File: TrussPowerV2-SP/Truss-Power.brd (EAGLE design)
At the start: 30.8 x 19 mm, 32 parts, among them J1 XF2L-0535-1, J2 XF2L-0535-1, Q1 ABM-16MHZ, SW1 LS12T2-T, SW2 EVQ11U09K, SW3 ESE31L11T, U2 TPS62200, X1 22-23-2021

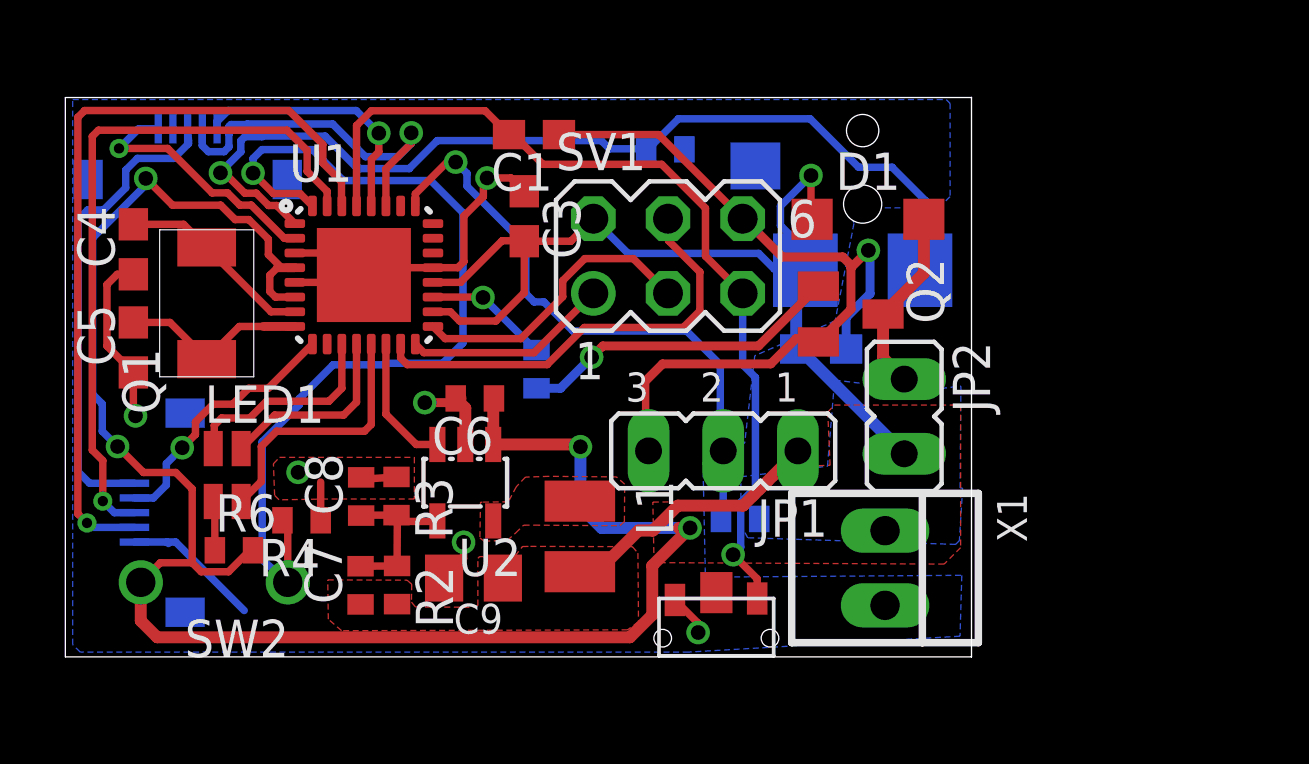
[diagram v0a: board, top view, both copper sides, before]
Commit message: Generate SP boards for Gen1
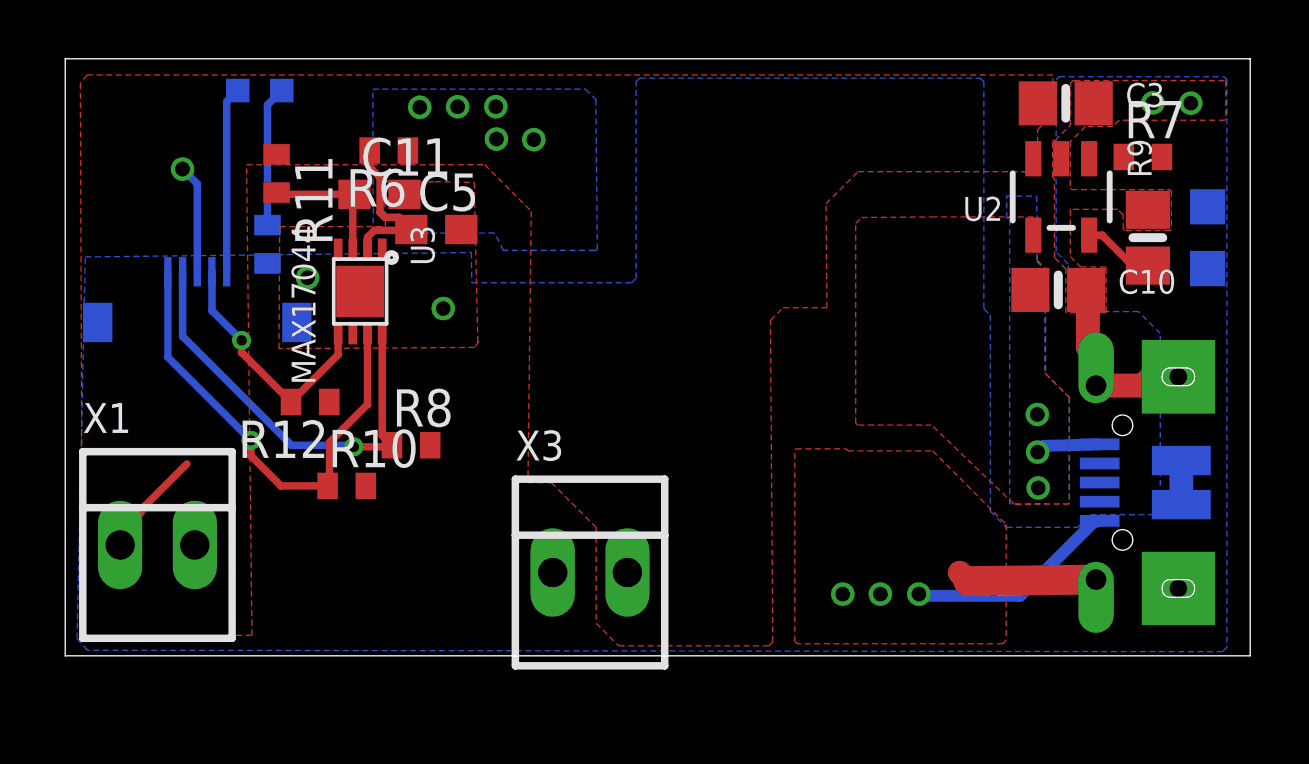
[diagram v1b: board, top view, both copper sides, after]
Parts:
- removed C1, C2: 100nF, rcl:C0603
- removed C4: 22pF, rcl:C0603
- removed C6: 4.7uF, rcl:C0402
- removed C7, C8: 100nF, rcl:C0402
- removed C9: 10uF, resistor:C0805K
- removed D1: (no value), diode:SOD123
- removed J2: XF2L-0535-1, adafruit:XF2L-0535-1
- removed JP1: MQ303B, jumper:JP2
- removed JP2: Solenoid, jumper:JP1
- removed L1: 10uH, resistor:L2825P
- removed Q1: ABM-16MHZ, NewPart:ABM-16MHZ
- removed Q2: (no value), semicon-smd-ipc:SOT23
- removed R1: 10K, resistor:R0402
- removed R2: 16K, resistor:R0402
- removed R3: 20K, resistor:R0402
- removed R4: 330, resistor:R0402
- removed R5: 2.2K, resistor:R0402
- removed SV1: (no value), con-lstb:MA03-2
- removed SW1: LS12T2-T, NewPart:LS12T2-T
- removed SW2: EVQ11U09K, NewPart:EVQ11U-09K
- removed SW3: ESE31L11T, NewPart:SWITCH
- removed U1: (no value), SparkFun-DigitalIC:MLF32-PAD
- added C10: 10µF, microbuilder:0805-NO
- added C11: 10nF, rcl:C0603
- added CHRG: ORANGE, microbuilder:CHIPLED_0805_NOOUTLINE
- added R10, R12, R8: 4.7K, resistor:R0402
- added R11: 180, resistor:R0402
- added R13: 330, resistor:R0402
- added R9: 2K, microbuilder:0805-NO
- added U3: MAX17044, NewPart:TDFN
- added X2: MicroB, microbuilder:4UCONN_20329
- added X3: 22-23-2021, con-molex:22-23-2021
- C3: value 100nF -> 10µF; device rcl:C0603 -> microbuilder:0805-NO
- C5: value 22pF -> 1uF
- J1: device adafruit:XF2L-0535-1 -> con-omron:XF2L-0535-1
- LED1: value LST-C19HE1WT -> (none); device led:LST-C19HE1WT -> led:CHIP-LED0603
- R7: value 330 -> 470
- U2: value TPS62200 -> MCP73831T-2ACI/OT; device NewPart:TPS62200 -> microbuilder:SOT23-5
- moved X1 24.8 mm to (3.14, 3.77), turned to 0 degrees
- moved U2 22.5 mm to (33.9, 15.6)
- moved C3 18.8 mm to (34.0, 18.8), turned to 0 degrees
- moved R7 16.2 mm to (36.7, 17.0), flipped to the top, turned to 0 degrees
- moved R6 14.6 mm to (11.0, 17.2), turned to 180 degrees
- moved LED1 13.1 mm to (6.62, 19.2), flipped to the bottom, turned to 90 degrees
- moved C5 11.1 mm to (12.6, 14.5), turned to 0 degrees
- moved J1 4.87 mm to (4.49, 11.2)
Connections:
- removed net DETSW: R7.1, SW3.3, U1.1
- removed net FB: C7.2, C8.1, R2.1, R3.2, U2.4
- removed net MISO: SV1.1, U1.16
- removed net MOSI: SV1.4, U1.15
- removed net MQ303_EN: U1.14, U2.3
- removed net N$10: Q2.1, R5.1
- removed net N$2: C4.2, Q1.P$2, U1.7
- removed net N$9: D1.A, JP2.1, Q2.3
- removed net PWRSW: R4.2, SW2.P$1, U1.32
- removed net REST: J2.2, U1.9
- removed net RGB-BLUE: LED1.2, U1.12
- removed net RGB-GRN: LED1.3, U1.13
- removed net RGB-RED: LED1.1, U1.11
- removed net RST: C1.2, SV1.5, SW1.P$2, U1.29
- removed net RX: J2.4, U1.30
- removed net SCK: SV1.3, U1.17
- removed net SOL: R5.2, U1.19
- removed net SW: L1.1, U2.5
- removed net TX: J2.3, U1.31
- removed net VBATSIM: J1.3, J2.1
- removed net VCC: C2.2, C3.2, C6.1, D1.C, JP2.2, R1.2, R6.2, SV1.2, SW2.P$2, SW3.4, U1.18, U1.20, U1.4, U1.6, U2.1, X1.1
- removed net VOUT: C7.1, C9.1, JP1.1, L1.2, R2.2
- new net ALRT: J1.2, R12.2, U3.5
- new net N$14: R9.1, U2.5
- new net N$4: LED1.C, R13.2
- new net N$6: CHRG.C, U2.1
- new net VBAT: C3.1, J1.3, R10.2, R11.1, R12.1, R6.1, R8.2, U2.3, X1.1, X3.2
- new net VBUS: C10.1, R7.2, U2.4, X2.VBUS
- net GND: now also C10.2, C11.2, C3.2, C5.2, R13.1, R9.2, U3.1, U3.4, U3.6, U3.9, X2.BASE@1, X2.BASE@2, X2.GND, X2.SPRT@1, X2.SPRT@2, X2.SPRT@3, X2.SPRT@4, X3.1; no longer C1.1, C2.1, C3.1, C4.1, C5.1, C6.2, C8.2, C9.2, J2.5, JP1.3, Q2.2, R3.1, R4.1, R7.2, SV1.6, SW1.P$1, U1.21, U1.3, U1.5, U1.PAD
- net LEDSOC: now also J1.1, LED1.A; no longer J1.5, U1.2
- net N$1: now also C5.1, R6.2, U3.2; no longer C5.2, Q1.P$1, U1.8
- net N$3: now also C11.1, R11.2, U3.3; no longer JP1.2, R1.1, U1.25
- net N$5: now also CHRG.A, R7.1; no longer LED1.4, R6.1
- net SCL: now also J1.5, R10.1, U3.7; no longer J1.1, U1.28
- net SDA: now also J1.4, R8.1, U3.8; no longer J1.2, U1.27
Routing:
- net VCC: track 96.6 -> 0.00 mm, vias 5 -> 0
- net GND: track 61.7 -> 19.8 mm
- net DETSW: track 33.0 -> 0.00 mm, vias 1 -> 0
- net PWRSW: track 31.3 -> 0.00 mm, vias 1 -> 0
- net RST: track 30.8 -> 0.00 mm, vias 1 -> 0
- net RX: track 26.9 -> 0.00 mm, vias 1 -> 0
- net TX: track 23.6 -> 0.00 mm, vias 1 -> 0
- net VBATSIM: track 16.3 -> 0.00 mm
- net N$3: track 20.6 -> 4.55 mm, vias 1 -> 0
- net MOSI: track 15.1 -> 0.00 mm
- net N$10: track 11.0 -> 0.00 mm, vias 1 -> 0
- net SCK: track 10.1 -> 0.00 mm
- net VOUT: track 9.38 -> 0.00 mm
- net RGB-GRN: track 8.94 -> 0.00 mm
- net REST: track 8.90 -> 0.00 mm, vias 1 -> 0
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- added copper zone on layer 1, net VBAT
- added copper zone on layer 16, net VBAT
- added copper zone on layer 1, net VBUS
- added copper zone on layer 16, net VBUS
- removed copper zone on layer 1, net SW
- removed copper zone on layer 1, net VCC
- removed copper zone on layer 16, net VCC
- removed copper zone on layer 1, net VOUT
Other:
- board size 30.8 x 19 mm -> 40.3 x 20.3 mm

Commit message: VBAT Polygon
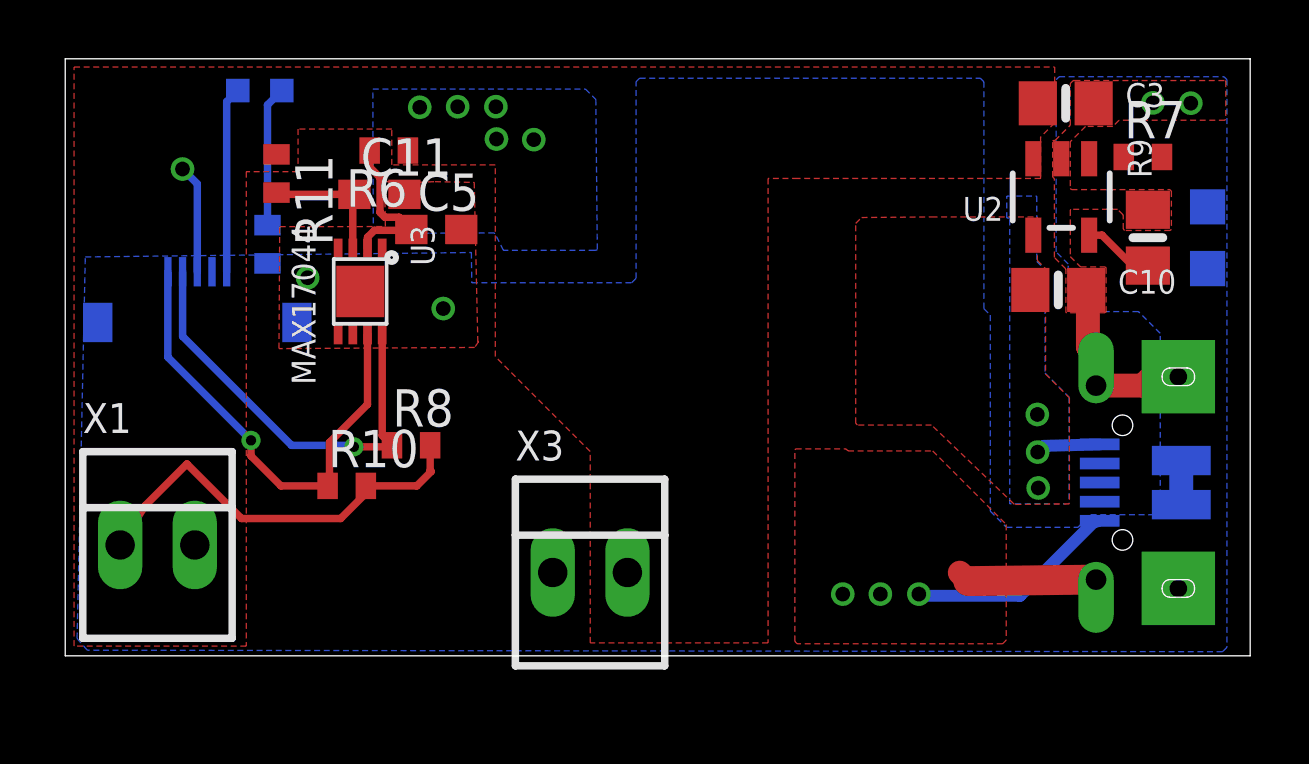
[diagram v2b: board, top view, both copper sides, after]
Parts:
- removed R12: 4.7K, resistor:R0402
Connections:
- removed net ALRT: J1.2, R12.2, U3.5
- net VBAT: no longer R12.1
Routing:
- net VBAT: track 7.30 -> 18.1 mm
- net ALRT: track 8.52 -> 0.00 mm, vias 1 -> 0
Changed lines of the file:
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@@
 <?xml version="1.0" encoding="utf-8"?>
 <!DOCTYPE eagle SYSTEM "eagle.dtd">
-<eagle version="9.2.2">
+<eagle version="9.1.3">
 <drawing>
 <settings>
@@
 <layer number="27" name="tValues" color="7" fill="1" visible="no" active="yes"/>
 <layer number="28" name="bValues" color="7" fill="1" visible="no" active="yes"/>
-<layer number="29" name="tStop" color="7" fill="3" visible="no" active="yes"/>
-<layer number="30" name="bStop" color="7" fill="6" visible="no" active="yes"/>
+<layer number="29" name="tStop" color="7" fill="3" visible="yes" active="yes"/>
+<layer number="30" name="bStop" color="7" fill="6" visible="yes" active="yes"/>
 <layer number="31" name="tCream" color="7" fill="4" visible="no" active="yes"/>
 <layer number="32" name="bCream" color="7" fill="5" visible="no" active="yes"/>
@@
 <attribute name="VALUE" x="5.2832" y="17.0434" size="1.27" layer="27" rot="R270"/>
 </element>
-<element name="R12" library="resistor" package="R0402" value="4.7K" x="8.3312" y="8.636" smashed="yes" rot="R180">
-<attribute name="NAME" x="8.9662" y="8.001" size="1.27" layer="25" rot="R180"/>
-<attribute name="VALUE" x="8.9662" y="10.541" size="1.27" layer="27" rot="R180"/>
-</element>
 <element name="C5" library="rcl" package="C0603" value="1uF" x="12.6238" y="14.5034" smashed="yes">
 <attribute name="NAME" x="11.9888" y="15.1384" size="1.27" layer="25"/>
@@
 <via x="14.65" y="18.68" extent="1-16" drill="0.5"/>
 <via x="14.67" y="17.58" extent="1-16" drill="0.5"/>
-<polygon width="0.254" layer="1" thermals="no">
-<vertex x="0.5864" y="0.6052"/>
-<vertex x="6.3522" y="0.7028"/>
-<vertex x="6.1696" y="16.7048"/>
-<vertex x="14.2722" y="16.7074"/>
-<vertex x="15.85390625" y="15.12569375"/>
-<vertex x="15.74" y="5.89"/>
-<vertex x="16.54" y="5.89"/>
-<vertex x="18.06" y="4.37"/>
-<vertex x="18.06" y="1.11"/>
-<vertex x="18.83" y="0.34"/>
-<vertex x="23.94" y="0.34"/>
-<vertex x="24.07" y="0.47"/>
-<vertex x="23.99" y="11.41"/>
-<vertex x="24.4212125" y="11.8412125"/>
-<vertex x="25.9113125" y="11.8412125"/>
-<vertex x="25.88" y="15.38"/>
-<vertex x="26.97" y="16.47"/>
-<vertex x="33.08" y="16.47"/>
-<vertex x="33.08" y="17.9"/>
-<vertex x="33.32" y="18.14"/>
-<vertex x="33.6" y="18.14"/>
-<vertex x="33.6" y="19.76"/>
-<vertex x="0.7466" y="19.76"/>
-<vertex x="0.5148" y="19.4774"/>
-</polygon>
 <contactref element="J1" pad="3"/>
 <contactref element="X1" pad="1"/>
 <contactref element="R11" pad="1"/>
 <wire x1="2.7178" y1="5.1054" x2="1.8678" y2="3.7708" width="0.254" layer="1"/>
-<wire x1="2.7178" y1="5.1054" x2="4.1402" y2="6.5278" width="0.254" layer="1"/>
+<wire x1="4.1402" y1="6.5278" x2="2.7178" y2="5.1054" width="0.254" layer="1"/>
 <via x="15.94" y="17.56" extent="1-16" drill="0.5"/>
 <via x="3.99" y="16.56" extent="1-16" drill="0.5"/>
@@
 <contactref element="R8" pad="2"/>
 <contactref element="R10" pad="2"/>
-<contactref element="R12" pad="1"/>
 <contactref element="X3" pad="2"/>
-<wire x1="10.226" y1="5.7802" x2="12.4152" y2="7.1628" width="0" layer="19" extent="1-1"/>
-<wire x1="8.9812" y1="8.636" x2="10.226" y2="5.7802" width="0" layer="19" extent="1-1"/>
-<wire x1="4.1402" y1="6.5278" x2="8.9812" y2="8.636" width="0" layer="19" extent="1-1"/>
+<polygon width="0.254" layer="1" thermals="no">
+<vertex x="0.3" y="0.33"/>
+<vertex x="0.3" y="20.03"/>
+<vertex x="33.66" y="20.03"/>
+<vertex x="33.66" y="18.13"/>
+<vertex x="33.18" y="17.65"/>
+<vertex x="33.18" y="16.24"/>
+<vertex x="24.93" y="16.24"/>
+<vertex x="23.91" y="16.24"/>
+<vertex x="23.91" y="0.44"/>
+<vertex x="17.86" y="0.44"/>
+<vertex x="17.86" y="5.98"/>
+<vertex x="17.86" y="6.95"/>
+<vertex x="14.63" y="10.18"/>
+<vertex x="14.63" y="16.7"/>
+<vertex x="11.11" y="16.7"/>
+<vertex x="11.11" y="17.92"/>
+<vertex x="7.92" y="17.92"/>
+<vertex x="7.92" y="16.47"/>
+<vertex x="6.16" y="16.47"/>
+<vertex x="6.16" y="0.33"/>
+</polygon>
+<wire x1="10.226" y1="5.7802" x2="11.9602" y2="5.7802" width="0.254" layer="1"/>
+<wire x1="11.9602" y1="5.7802" x2="12.45" y2="6.27" width="0.254" layer="1"/>
+<wire x1="12.45" y1="6.27" x2="12.4152" y2="6.3048" width="0.254" layer="1"/>
+<wire x1="12.4152" y1="6.3048" x2="12.4152" y2="7.1628" width="0.254" layer="1"/>
+<wire x1="10.226" y1="5.7802" x2="10.226" y2="5.526" width="0.254" layer="1"/>
+<wire x1="10.226" y1="5.526" x2="9.37" y2="4.67" width="0.254" layer="1"/>
+<wire x1="9.37" y1="4.67" x2="5.998" y2="4.67" width="0.254" layer="1"/>
+<wire x1="5.998" y1="4.67" x2="4.1402" y2="6.5278" width="0.254" layer="1"/>
 </signal>
 <signal name="VBUS">
@@
 </polygon>
 <contactref element="R7" pad="2"/>
-<wire x1="32.932" y1="14.3099" x2="37.31" y2="16.97" width="0" layer="19" extent="1-1"/>
+<wire x1="37.31" y1="16.97" x2="32.932" y2="14.3099" width="0" layer="19" extent="1-1"/>
 </signal>
 <signal name="SCL">
@@
 <wire x1="9.783" y1="15.643" x2="9.8386" y2="15.6986" width="0.254" layer="1"/>
 </signal>
-<signal name="ALRT">
-<contactref element="U3" pad="5"/>
-<contactref element="R12" pad="2"/>
-<wire x1="9.283" y1="10.9452" x2="9.283" y2="10.2378" width="0.254" layer="1"/>
-<wire x1="7.6812" y1="8.636" x2="9.283" y2="10.2378" width="0.254" layer="1"/>
-<contactref element="J1" pad="2"/>
-<wire x1="4.9926" y1="13.0658" x2="4.9926" y2="11.7374" width="0.254" layer="16"/>
-<wire x1="4.9926" y1="11.7374" x2="6" y2="10.73" width="0.254" layer="16"/>
-<via x="6" y="10.73" extent="1-16" drill="0.35"/>
-<wire x1="6" y1="10.73" x2="6" y2="10.3172" width="0.254" layer="1"/>
-<wire x1="6" y1="10.3172" x2="7.6812" y2="8.636" width="0.254" layer="1"/>
-</signal>
 <signal name="LEDSOC">
 <contactref element="J1" pad="1"/>
@@
 <contactref element="R7" pad="1"/>
 <contactref element="CHRG" pad="A"/>
-<wire x1="38.862" y1="13.174" x2="36.01" y2="16.97" width="0" layer="19" extent="1-16"/>
+<wire x1="36.01" y1="16.97" x2="38.862" y2="13.174" width="0" layer="19" extent="1-16"/>
 </signal>
 <signal name="N$6">

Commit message: LED moved
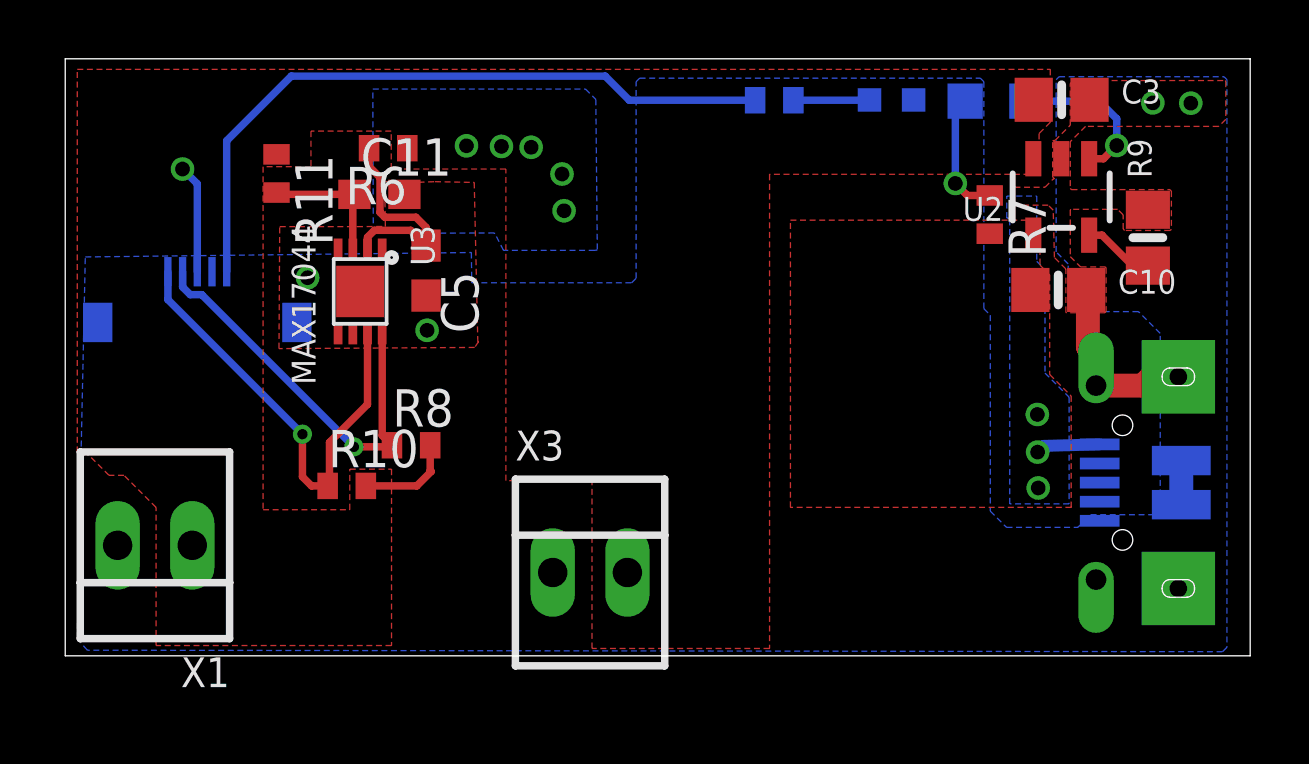
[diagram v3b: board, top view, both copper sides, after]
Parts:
- moved LED1 21.5 mm to (28.1, 18.9)
- moved R13 17.9 mm to (24.1, 18.9), turned to 0 degrees
- moved CHRG 8.57 mm to (31.7, 18.9), turned to 90 degrees
- moved R7 5.57 mm to (31.4, 15.0), turned to 270 degrees
- moved C5 1.44 mm to (12.3, 13.1), turned to 270 degrees
- moved C3 0.18 mm to (33.9, 18.9)
- moved X1 0.09 mm to (3.05, 3.76), turned to 180 degrees
- moved R6 0.08 mm to (11.0, 17.3)
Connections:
- net GND: now also LED1.C; no longer R13.1
- net LEDSOC: now also R13.2; no longer LED1.A
- net N$4: now also LED1.A, R13.1; no longer LED1.C, R13.2
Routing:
- net LEDSOC: track 6.32 -> 23.7 mm
- net GND: track 19.8 -> 7.82 mm, vias 7 -> 4
- net VBAT: track 18.1 -> 7.29 mm
- net N$6: track 0.00 -> 5.34 mm, vias 0 -> 1
- net N$5: track 0.00 -> 4.28 mm, vias 0 -> 1
- net N$4: track 4.78 -> 2.59 mm
- net N$1: track 5.55 -> 7.43 mm
- net SDA: track 14.8 -> 13.8 mm
- net SCL: track 16.3 -> 15.6 mm
